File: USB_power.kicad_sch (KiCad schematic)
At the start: 13 parts, among them J1 PWR_IN, J2 USB_A

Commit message: 名前変更
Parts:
- added C10: 10uF, Capacitor_SMD:C_0805_2012Metric, symbol Device:C
- added C6, C7: 10uF, Capacitor_SMD:C_0805_2012Metric, symbol Device:C_Small
- added C8, C9: 1uF, Capacitor_SMD:C_0805_2012Metric, symbol Device:C_Small
- added J3: PWR_IN, Connector_AMASS:AMASS_XT60-M_1x02_P7.20mm_Vertical, symbol Connector:Conn_01x02_Socket
- added MD2: OKL-T_6-W12N-C, Pi_Header:MURATA_OKL-T-6-W12N-C_0, symbol OKL-T_6-W12N-C:OKL-T_6-W12N-C
- added R10: 200R, Resistor_SMD:R_0805_2012Metric, symbol Device:R
- added R6, R9: 1k, Resistor_SMD:R_0805_2012Metric, symbol Device:R
- added R7: 330R, Resistor_SMD:R_0805_2012Metric, symbol Device:R
- added R8: 10R, Resistor_SMD:R_0805_2012Metric, symbol Device:R
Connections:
- net +5V: now also C10.1, MD2.4 (VOUT), MD2.5 (SENSE), R9.1
- net +BATT: now also C6.1, C7.1, C8.1, C9.1, J3.1 (Pin_1), MD2.2 (VIN)
- net GND: now also C10.2, C6.2, C7.2, C8.2, C9.2, J3.2 (Pin_2), MD2.1 (~{ON}/OFF_CONTROL), MD2.3 (1_GROUND), MD2.7 (2_GROUND), R10.2, R8.2
- new net: R10.1, R9.2
- new net: MD2.6 (TRIM), R6.1
- new net: R7.2, R8.1
- new net: R6.2, R7.1
- no-connect marks 7 -> 12

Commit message: USB-Cに変更
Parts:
- removed J2: USB_A, Connector_USB:USB_A_CONNFLY_DS1095-WNR0, symbol Connector:USB_A
- added J2: USB_A_Stacked, symbol Connector:USB_A_Stacked
- added J5: USB_C_Receptacle_PowerOnly_6P, symbol Connector:USB_C_Receptacle_PowerOnly_6P
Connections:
- net +5V: now also J5.A9 (VBUS), J5.B9 (VBUS); no longer C10.1, MD2.4 (VOUT), MD2.5 (SENSE), R9.1
- net GND: now also J5.A12 (GND), J5.B12 (GND), J5.S1 (SHIELD); no longer C10.2, MD2.3 (1_GROUND), MD2.7 (2_GROUND), R10.2, R8.2
- new net +5VA: C10.1, J2.1 (VBUS1), J2.5 (VBUS2), MD2.4 (VOUT), MD2.5 (SENSE), R9.1
- new net GNDA: C10.2, J2.4 (GND1), J2.8 (GND2), J2.9 (Shield), MD2.3 (1_GROUND), MD2.7 (2_GROUND), R10.2, R8.2
- no-connect marks 12 -> 16

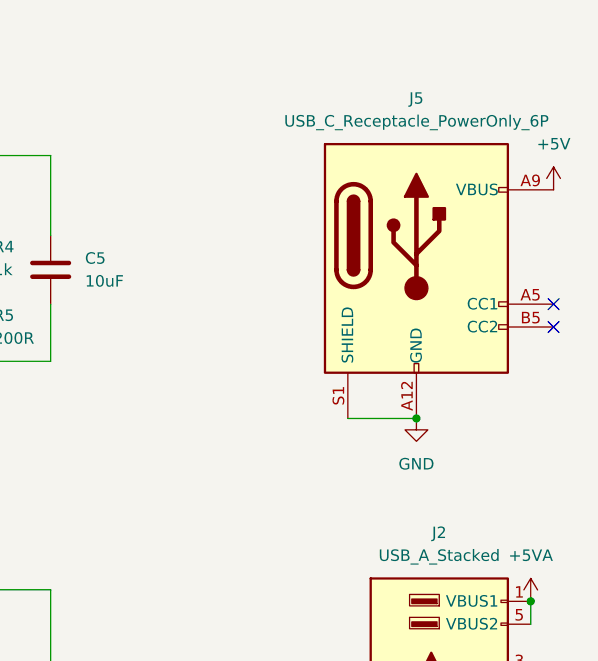
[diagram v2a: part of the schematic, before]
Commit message: USB-Cにフップリ割り当て
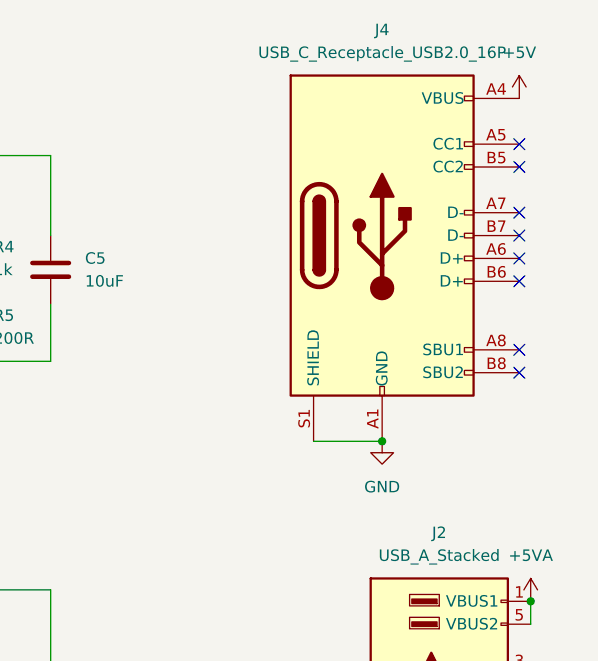
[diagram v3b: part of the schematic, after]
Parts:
- removed J5: USB_C_Receptacle_PowerOnly_6P, symbol Connector:USB_C_Receptacle_PowerOnly_6P
- added J4: USB_C_Receptacle_USB2.0_16P, Connector_USB:USB_C_Receptacle_GCT_USB4105-xx-A_16P_TopMnt_Horizontal, symbol Connector:USB_C_Receptacle_USB2.0_16P
- J2: footprint (none) -> Connector_USB:USB_A_CUI_UJ2-ADH-TH_Horizontal_Stacked
- MD1, MD2: footprint Pi_Header:MURATA_OKL-T-6-W12N-C_0 -> USB_power:MURATA_OKL-T-6-W12N-C_0
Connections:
- net +5V: now also J4.A4 (VBUS), J4.A9 (VBUS), J4.B4 (VBUS), J4.B9 (VBUS)
- net GND: now also J4.A1 (GND), J4.A12 (GND), J4.B1 (GND), J4.B12 (GND), J4.S1 (SHIELD)
- no-connect marks 16 -> 22

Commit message: 配線完了
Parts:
- removed C2, C6, C7: 10uF, Capacitor_SMD:C_0805_2012Metric, symbol Device:C_Small
- removed C3, C4, C8, C9: 1uF, Capacitor_SMD:C_0805_2012Metric, symbol Device:C_Small
- added C2: 22uF, Capacitor_SMD:C_0805_2012Metric, symbol Device:C
- C1: value 10uF -> 22uF
- J3: value PWR_IN -> Power_check; footprint Connector_AMASS:AMASS_XT60-M_1x02_P7.20mm_Vertical -> (none)
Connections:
- net +BATT: now also C2.1
- net GND: now also C10.2, J2.4 (GND1), J2.8 (GND2), MD2.3 (1_GROUND), MD2.7 (2_GROUND), R10.2, R8.2, C2.2; no longer J4.S1 (SHIELD)
- net +5VA renamed +5VP
- removed net GNDA: C10.2, J2.4 (GND1), J2.8 (GND2), J2.9 (Shield), MD2.3 (1_GROUND), MD2.7 (2_GROUND), R10.2, R8.2
- no-connect marks 22 -> 24
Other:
- moved on the sheet: C1, J1

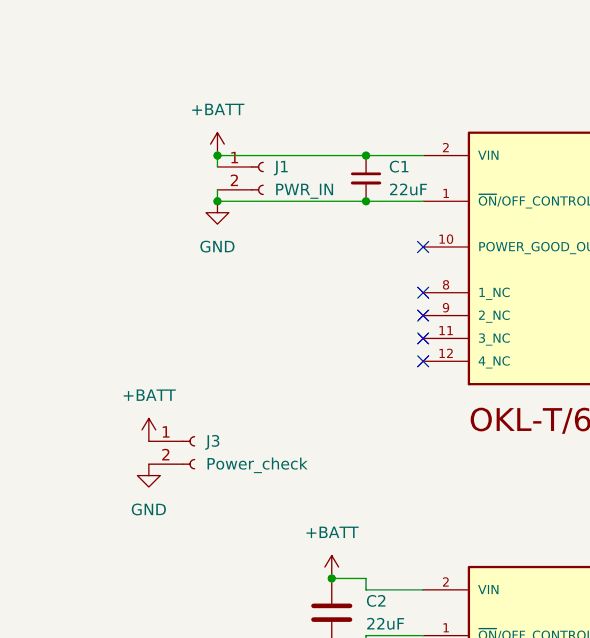
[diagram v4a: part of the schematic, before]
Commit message: XT60の向きなおした
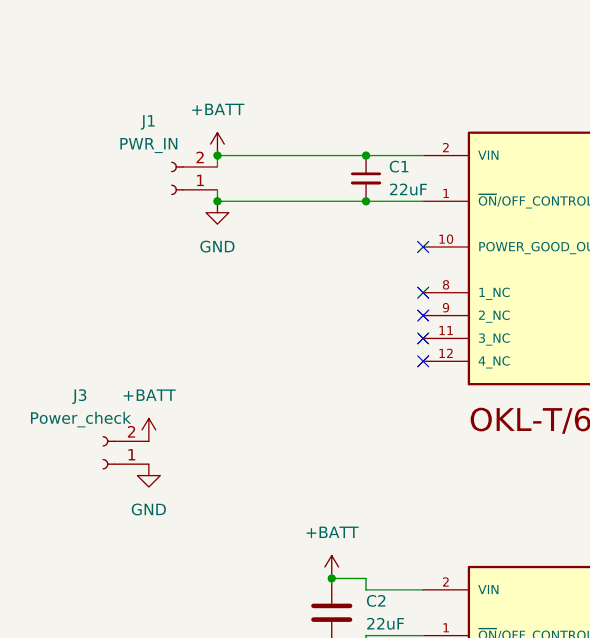
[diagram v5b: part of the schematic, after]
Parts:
- J3: footprint (none) -> Connector_JST:JST_XA_B02B-XASK-1_1x02_P2.50mm_Vertical
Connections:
- net +BATT: now also J1.2 (Pin_2), J3.2 (Pin_2); no longer J1.1 (Pin_1), J3.1 (Pin_1)
- net GND: now also J1.1 (Pin_1), J3.1 (Pin_1); no longer J1.2 (Pin_2), J3.2 (Pin_2)
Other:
- moved on the sheet: J1, J3
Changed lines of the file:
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@@
 	(symbol
 		(lib_id "Connector:Conn_01x02_Socket")
-		(at 49.53 91.44 0)
-		(unit 1)
-		(exclude_from_sim no)
-		(in_bom yes)
-		(on_board yes)
-		(dnp no)
-		(fields_autoplaced yes)
+		(at 39.37 93.98 180)
+		(unit 1)
+		(exclude_from_sim no)
+		(in_bom yes)
+		(on_board yes)
+		(dnp no)
 		(property "Reference" "J3"
-			(at 50.8 91.4399 0)
-			(effects
-				(font
-					(size 1.27 1.27)
-				)
-				(justify left)
+			(at 36.83 86.36 0)
+			(effects
+				(font
+					(size 1.27 1.27)
+				)
 			)
 		)
 		(property "Value" "Power_check"
-			(at 50.8 93.9799 0)
-			(effects
-				(font
-					(size 1.27 1.27)
-				)
-				(justify left)
-			)
-		)
-		(property "Footprint" ""
-			(at 49.53 91.44 0)
+			(at 36.83 88.9 0)
+			(effects
+				(font
+					(size 1.27 1.27)
+				)
+			)
+		)
+		(property "Footprint" "Connector_JST:JST_XA_B02B-XASK-1_1x02_P2.50mm_Vertical"
+			(at 39.37 93.98 0)
 			(effects
 				(font
@@
 		)
 		(property "Datasheet" "~"
-			(at 49.53 91.44 0)
+			(at 39.37 93.98 0)
 			(effects
 				(font
@@
 		)
 		(property "Description" "Generic connector, single row, 01x02, script generated"
-			(at 49.53 91.44 0)
+			(at 39.37 93.98 0)
 			(effects
 				(font
@@
 	(symbol
 		(lib_id "Connector:Conn_01x02_Socket")
-		(at 57.15 60.96 0)
-		(unit 1)
-		(exclude_from_sim no)
-		(in_bom yes)
-		(on_board yes)
-		(dnp no)
-		(fields_autoplaced yes)
+		(at 46.99 63.5 180)
+		(unit 1)
+		(exclude_from_sim no)
+		(in_bom yes)
+		(on_board yes)
+		(dnp no)
 		(property "Reference" "J1"
-			(at 58.42 60.9599 0)
-			(effects
-				(font
-					(size 1.27 1.27)
-				)
-				(justify left)
+			(at 44.45 55.88 0)
+			(effects
+				(font
+					(size 1.27 1.27)
+				)
 			)
 		)
 		(property "Value" "PWR_IN"
-			(at 58.42 63.4999 0)
-			(effects
-				(font
-					(size 1.27 1.27)
-				)
-				(justify left)
+			(at 44.45 58.42 0)
+			(effects
+				(font
+					(size 1.27 1.27)
+				)
 			)
 		)
 		(property "Footprint" "Connector_AMASS:AMASS_XT60-M_1x02_P7.20mm_Vertical"
-			(at 57.15 60.96 0)
+			(at 46.99 63.5 0)
 			(effects
 				(font
@@
 		)
 		(property "Datasheet" "~"
-			(at 57.15 60.96 0)
+			(at 46.99 63.5 0)
 			(effects
 				(font
@@
 		)
 		(property "Description" "Generic connector, single row, 01x02, script generated"
-			(at 57.15 60.96 0)
-			(effects
-				(font
+			(at 46.99 63.5 0)
+			(effects
+				(font

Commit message: 穴あけなど
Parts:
- removed J2: USB_A_Stacked, Connector_USB:USB_A_CUI_UJ2-ADH-TH_Horizontal_Stacked, symbol Connector:USB_A_Stacked
- added H1, H2, H3, H4: MountingHole, MountingHole:MountingHole_3.2mm_M3, symbol Mechanical:MountingHole
- added J5, J6: USB_A, Connector_USB:USB_A_CONNFLY_DS1095-WNR0, symbol Connector:USB_A
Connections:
- net +5VP: now also J5.1 (VBUS), J6.1 (VBUS)
- net GND: now also J5.4 (GND), J6.4 (GND)
- no-connect marks 24 -> 25

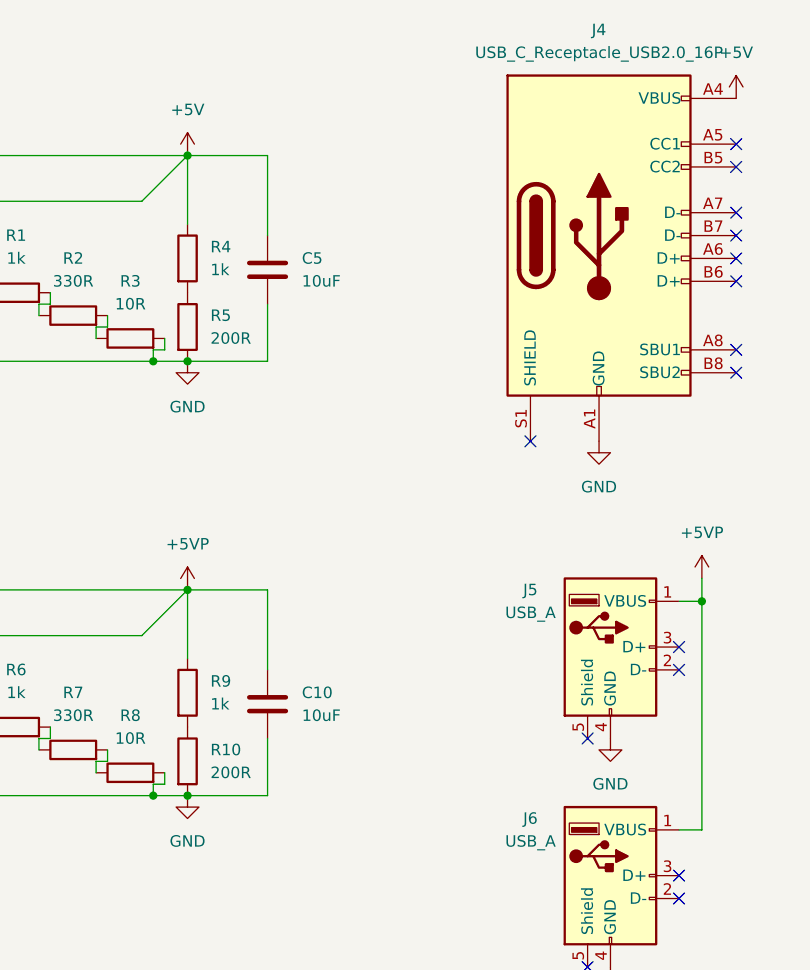
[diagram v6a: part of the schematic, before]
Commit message: 5V確認用LED追加
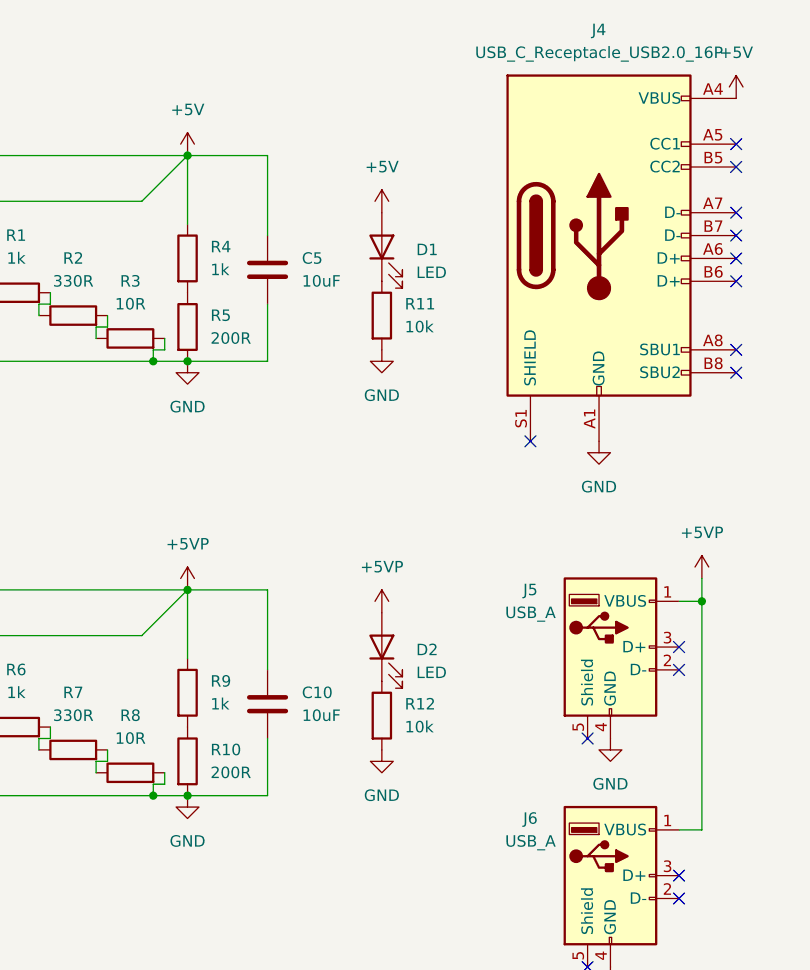
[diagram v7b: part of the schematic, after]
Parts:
- added D1, D2: LED, LED_SMD:LED_0603_1608Metric, symbol Device:LED
- added R11, R12: 10k, Resistor_SMD:R_0805_2012Metric, symbol Device:R
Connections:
- net +5V: now also D1.2 (A)
- net +5VP: now also D2.2 (A)
- net GND: now also R11.2, R12.2
- new net: D2.1 (K), R12.1
- new net: D1.1 (K), R11.1

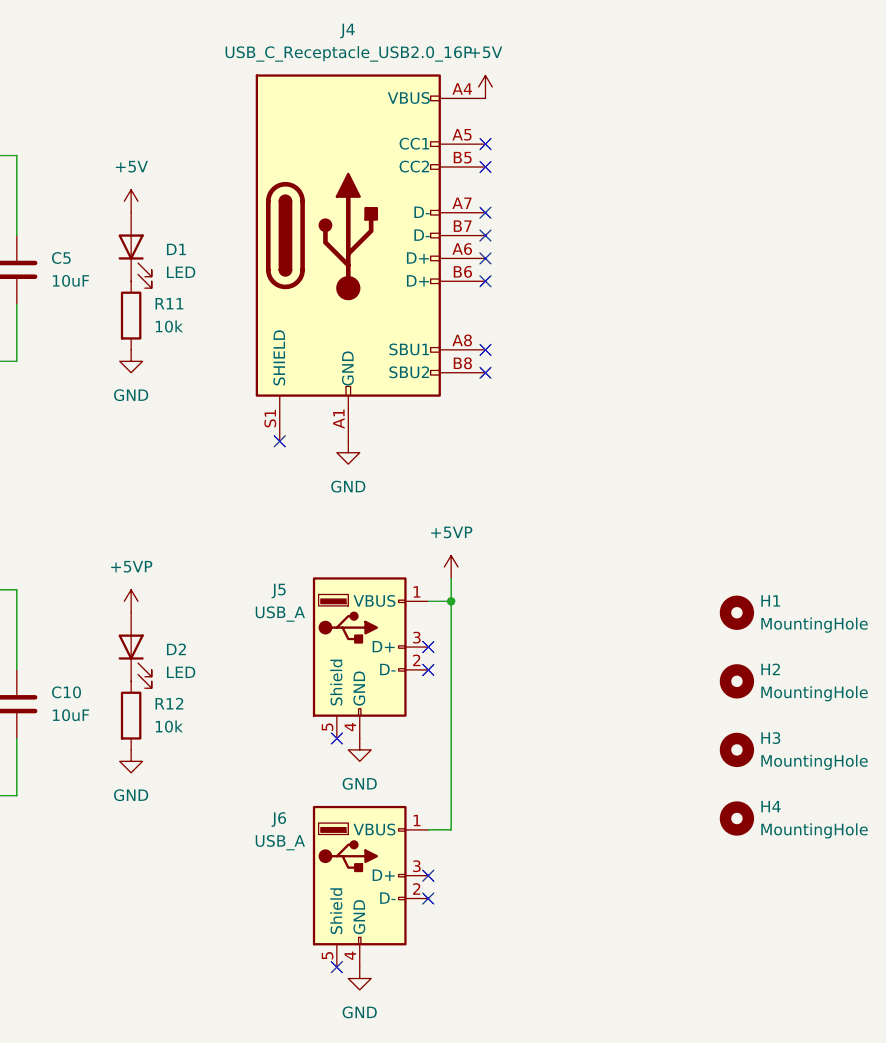
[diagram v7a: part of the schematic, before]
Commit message: USBコネクタ構成変更: stucked_A、A、C
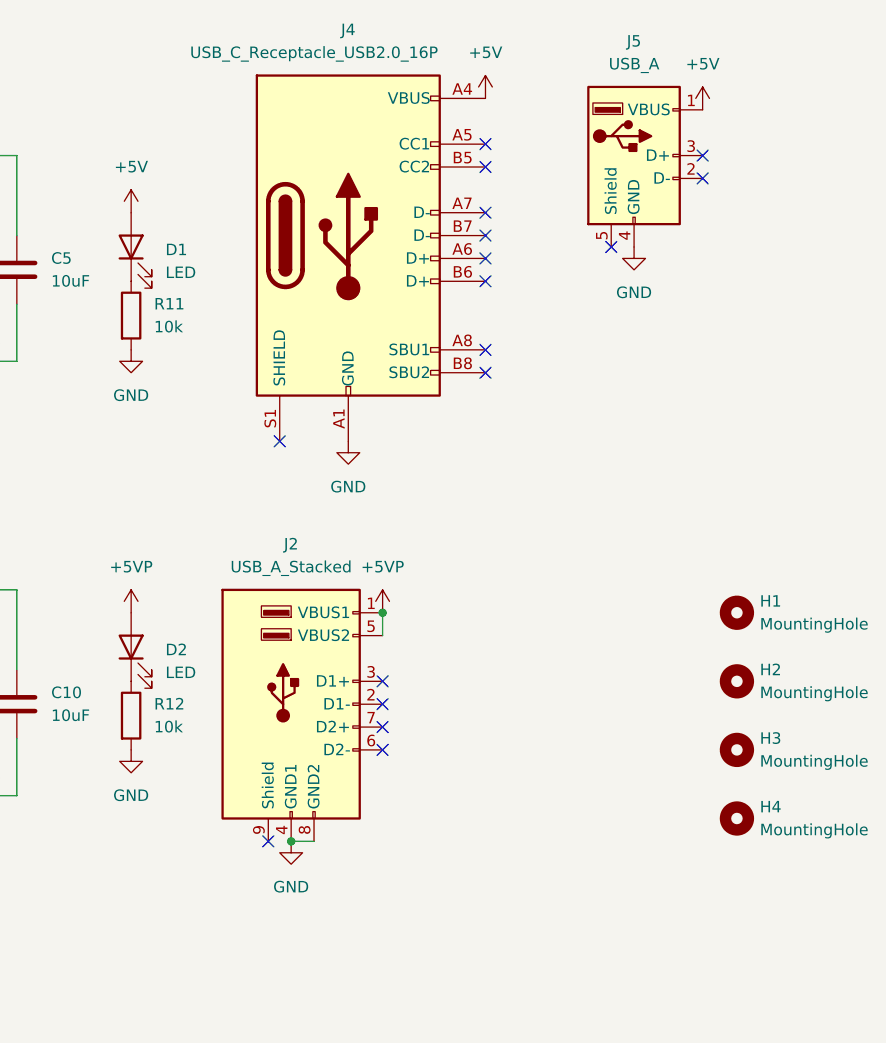
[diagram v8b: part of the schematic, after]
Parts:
- removed J6: USB_A, Connector_USB:USB_A_CONNFLY_DS1095-WNR0, symbol Connector:USB_A
- added J2: USB_A_Stacked, Connector_USB:USB_A_CUI_UJ2-ADH-TH_Horizontal_Stacked, symbol Connector:USB_A_Stacked
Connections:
- net +5V: now also J5.1 (VBUS)
- net +5VP: now also J2.1 (VBUS1), J2.5 (VBUS2); no longer J5.1 (VBUS)
- net GND: now also J2.4 (GND1), J2.8 (GND2)
- no-connect marks 25 -> 27
